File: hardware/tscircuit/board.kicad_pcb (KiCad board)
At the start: 2 copper layers, 400 x 300 mm, 174 parts, among them SW1 10mΩ, SW11 10mΩ, SW12 10mΩ, SW13 10mΩ

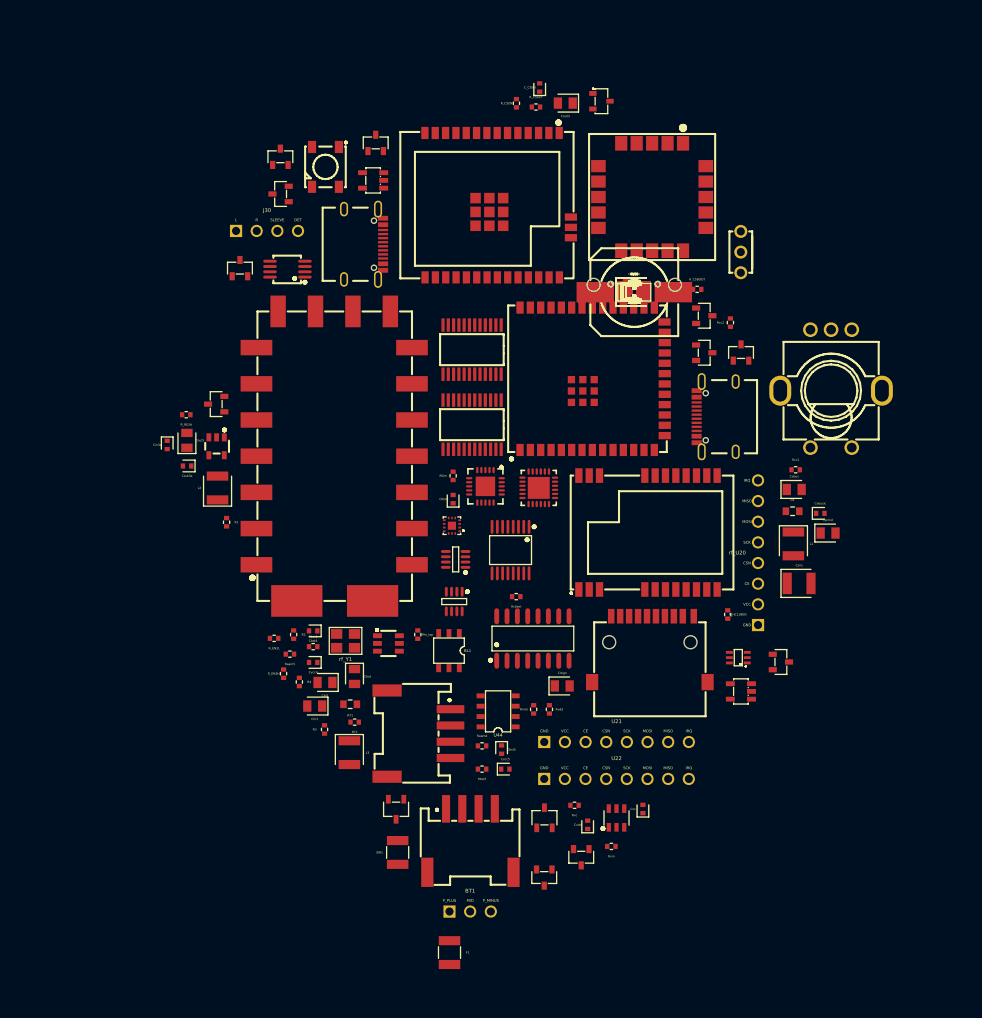
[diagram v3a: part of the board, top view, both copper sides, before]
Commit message: hardware(stage1): add display FPC, antenna u.FL, full controls + 3rd PCA9555
Completes the schematic's missing connectors + controls:
- Display FPC connector C19273968 (LCD_*/SPI/power/backlight wired;
  backlight LED nets go to the Stage-3 driver; touch pins NC).
- 3× u.FL C2987682 for the bare radios (CC1101/SA868/Si4732),
  pin2=signal; Si4732 whip shares FM/AM via a coupling cap.
- Master switch: proxy resistor -> real SPDT C496164 (COM=pin2).
- Full nav control set: D-pad (5 tactiles) + BACK + OPTIONS + STOP +
  F1 + F2 on a 3rd PCA9555 (U14, 0x22); PTT stays on U13.

191 footprints (was 174). All display + bare-radio-antenna nets now
connected. Remaining danglers are expected: ANT_LoRa (E22 module has
its own IPEX), 7× TXDET_* (envelope detectors = Stage 3), WS2812_DOUT
(intentional NC). Still placeholders for Stage 2: buttons/switch parts
picked but mic/speaker/buzzer/jack/holder/balun/matching/TVS/fuse remain.

Co-Authored-By: Claude Opus 4.8 <noreply@anthropic.com>
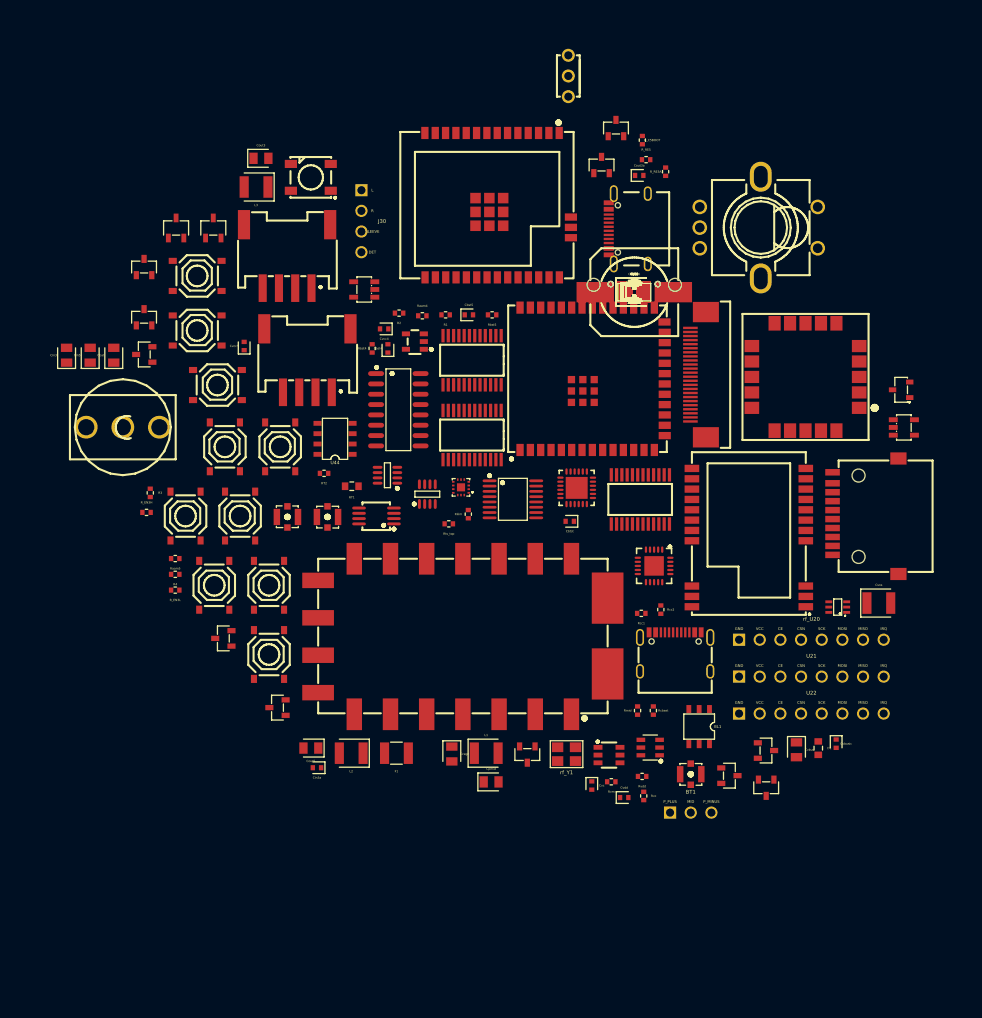
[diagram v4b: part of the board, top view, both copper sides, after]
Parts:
- added Ccpl_si: 100pF, tscircuit:capacitor_cap0402, F.Cu at (100.0, 100.0)
- added Cu14: 100nF, tscircuit:capacitor_cap0402, F.Cu at (100.0, 100.0)
- added J_ANT_CC: , tscircuit:chip, F.Cu at (106.9, 159.3)
- added J_ANT_SI: , tscircuit:chip, F.Cu at (57.4, 127.6)
- added J_ANT_UHF: , tscircuit:chip, F.Cu at (62.3, 127.6)
- added J_LCD: , tscircuit:chip, F.Cu at (108.2, 110.1)
- added SW_BACK: , tscircuit:chip, F.Cu at (46.3, 104.7)
- added SW_DN: , tscircuit:chip, F.Cu at (51.5, 127.5)
- added SW_F1: , tscircuit:chip, F.Cu at (55.1, 144.5)
- added SW_F2: , tscircuit:chip, F.Cu at (48.4, 136.0)
- added SW_LF: , tscircuit:chip, F.Cu at (49.7, 119.0)
- added SW_OK: , tscircuit:chip, F.Cu at (48.8, 111.4)
- added SW_OPT: , tscircuit:chip, F.Cu at (46.3, 98.0)
- added SW_RT: , tscircuit:chip, F.Cu at (55.1, 136.0)
- added SW_STOP: , tscircuit:chip, F.Cu at (44.8, 127.5)
- added SW_UP: , tscircuit:chip, F.Cu at (56.5, 119.0)
- added U14: , tscircuit:chip, F.Cu at (80.1, 117.6)
- SW1: value 10mΩ -> (none); footprint tscircuit:resistor_res1210 -> tscircuit:chip
- moved Q54 97.9 mm to (116.2, 160.9), turned to 90 degrees
- moved Q56 92.1 mm to (39.7, 96.9), turned to -90 degrees
- moved D40 83.2 mm to (48.2, 92.1)
- moved D41 76.4 mm to (43.7, 92.1), turned to -90 degrees
- moved J41 75.4 mm to (57.3, 95.6), turned to 180 degrees
- moved Q55 73.5 mm to (39.7, 103.1)
- moved L3 70.5 mm to (53.5, 87.1), turned to 180 degrees
- moved Cout3a 66.1 mm to (100.6, 85.6), turned to 0 degrees
- moved R_RE3A 66.1 mm to (103.9, 85.2), turned to 90 degrees
- moved SW1 62.2 mm to (37.1, 116.6)
- moved Cvcc5 61.1 mm to (52.0, 106.6), turned to 90 degrees
- moved Q57 57.6 mm to (86.9, 156.8), turned to 90 degrees
- moved Rbst5 55.9 mm to (82.5, 102.8)
- moved Q53 55.1 mm to (49.5, 142.6)
- moved Q52 54.2 mm to (56.1, 151.1), turned to 0 degrees
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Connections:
- F1 pad 2: .F1 > .pin2 to .SW1 > .pin1 -> .F1 > .pin2 to .SW1 > .pin2
- SW1 pad 1: .F1 > .pin2 to .SW1 > .pin1 -> BAT
- SW1 pad 2: BAT -> .F1 > .pin2 to .SW1 > .pin2
